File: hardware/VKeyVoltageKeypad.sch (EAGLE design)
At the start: 43 parts, among them IC1 OPAMP-DUALU

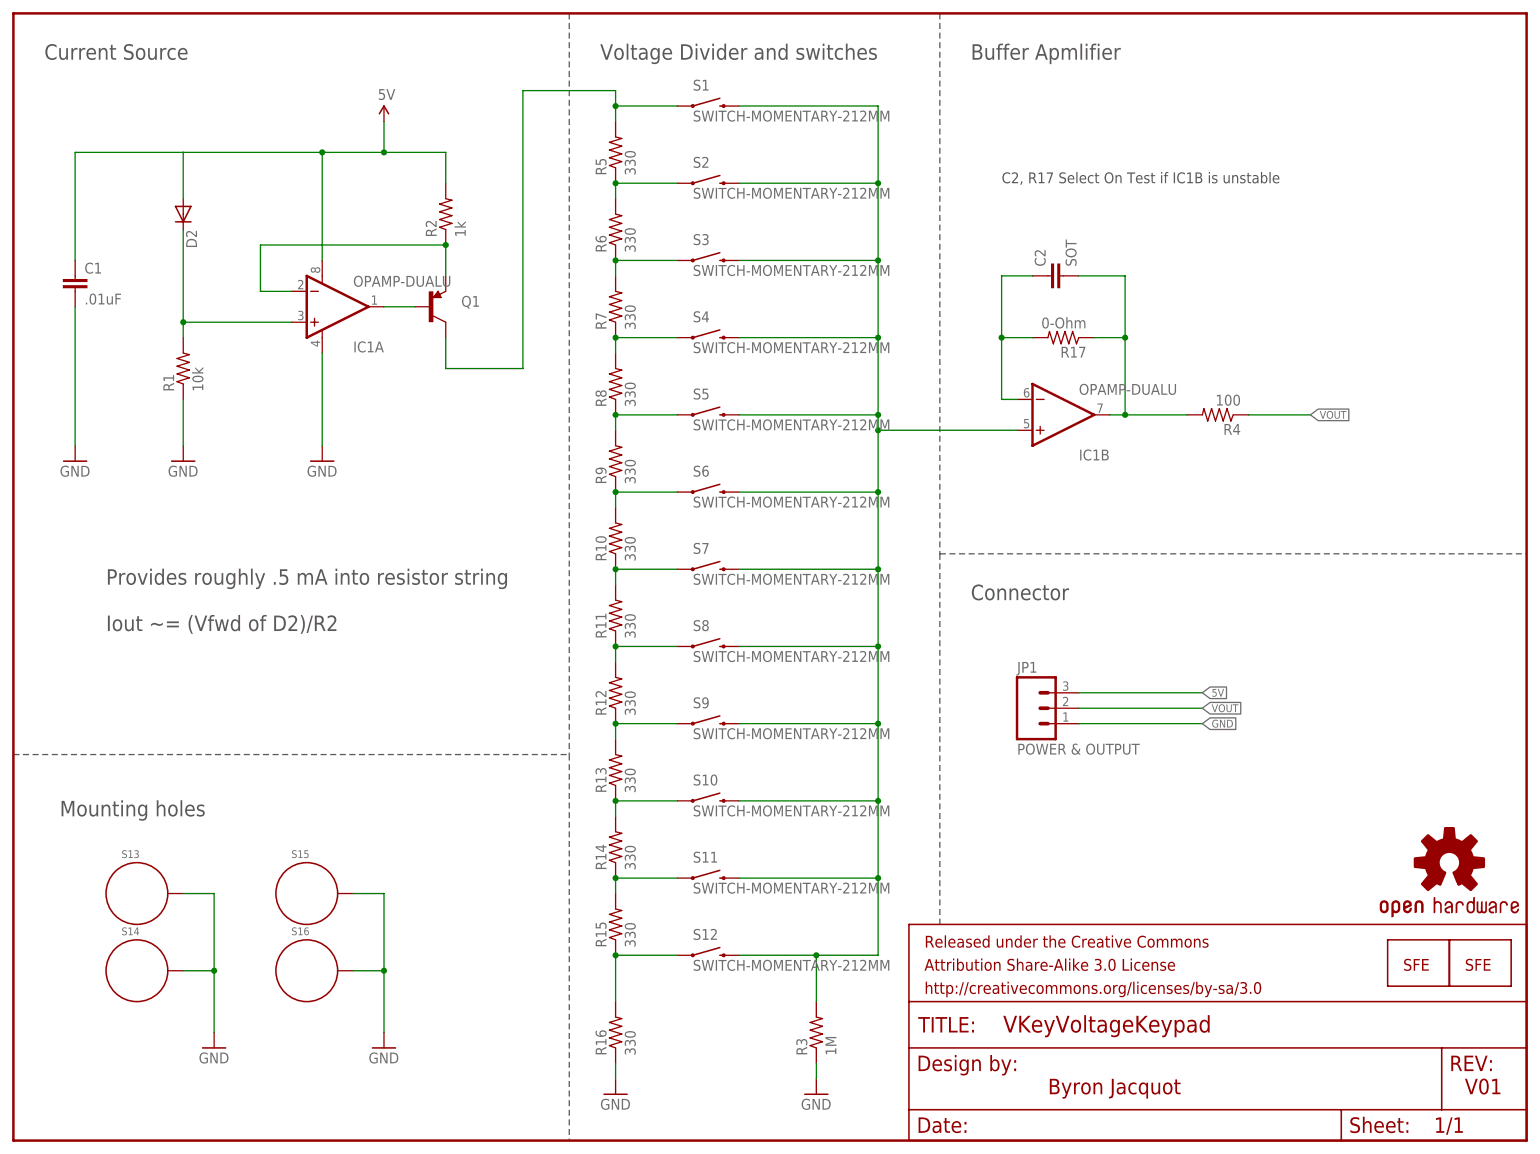
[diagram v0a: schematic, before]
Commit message: Dressing up based on prototype review.
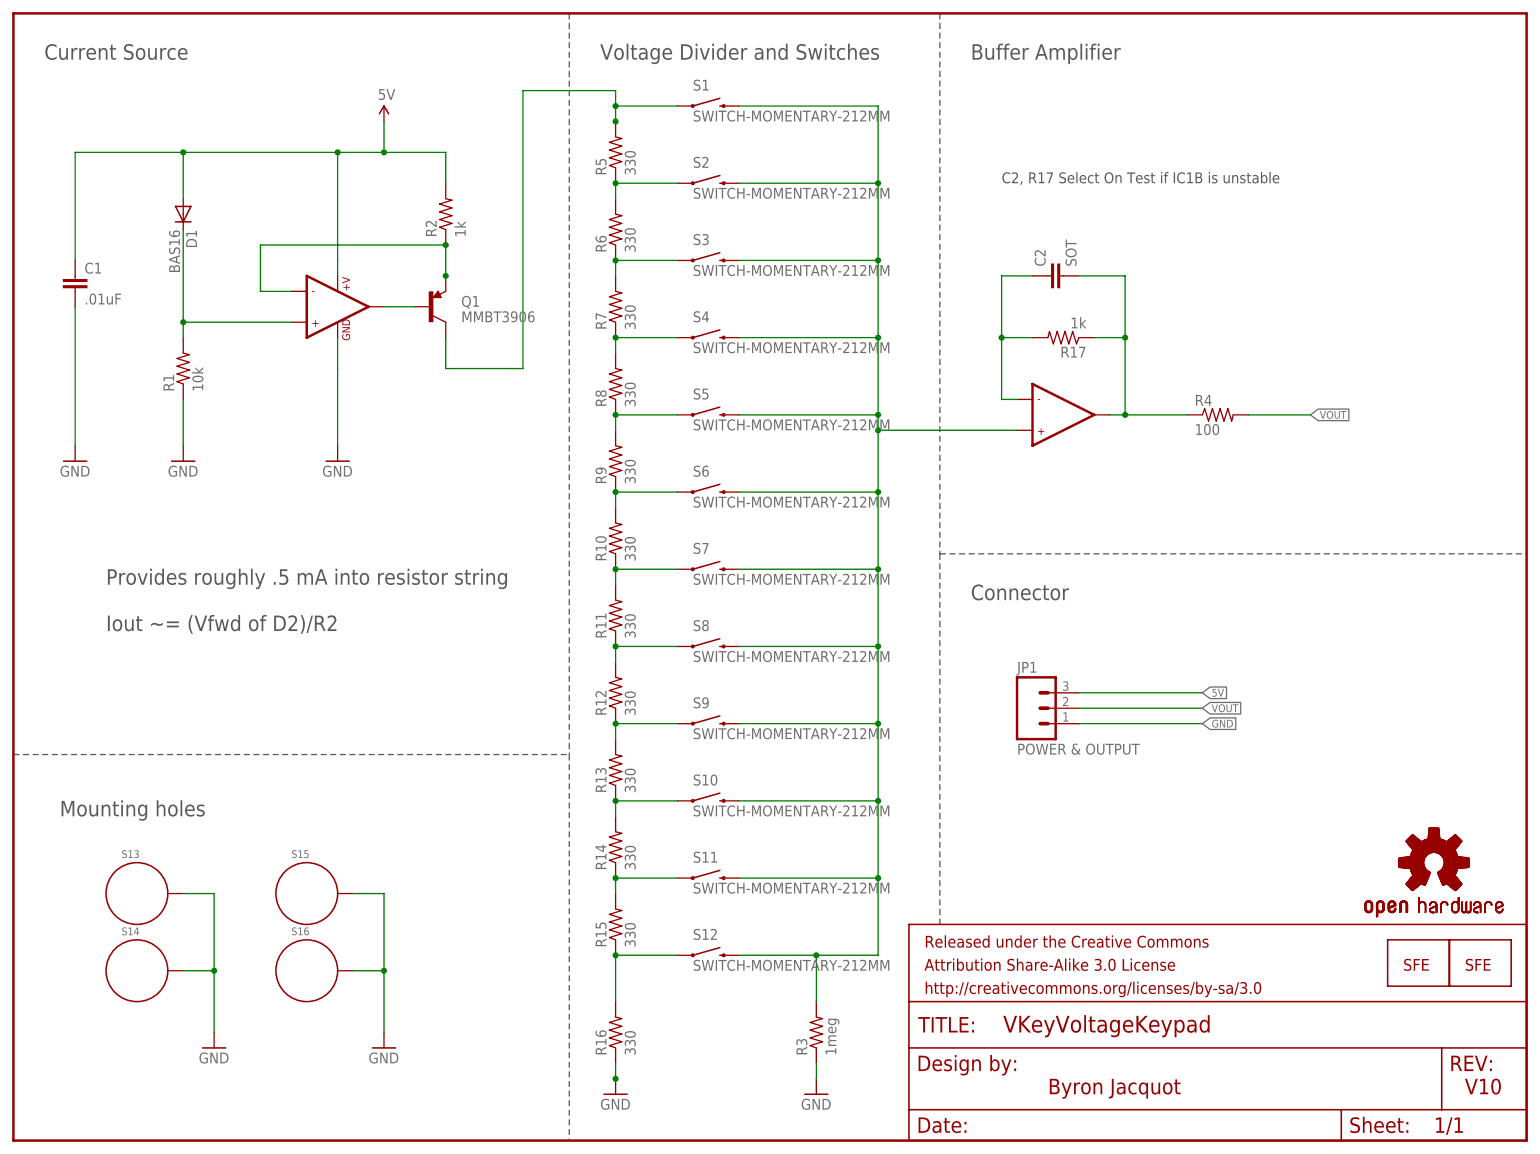
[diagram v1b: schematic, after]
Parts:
- removed D2: (no value), SparkFun-DiscreteSemi:DIODESMA
- removed IC1: OPAMP-DUALU, SparkFun-AnalogIC:OPAMP-DUALU
- added D1: BAS16, SparkFun-DiscreteSemi:DIODESOD
- added LOGO4: OSHW-LOGOL, SparkFun-Aesthetics:OSHW-LOGOL
- added U1: LMV358, SparkFun-AnalogIC:LMV358
- JP1: device SparkFun-Connectors:M03JST-PTH -> SparkFun-Connectors:M031X03_NO_SILK
- Q1: value (none) -> MMBT3906
- R1: device SparkFun-Passives:RESISTOR0603-RES -> SparkFun-Resistors:10KOHM1/10W1%(0603)0603
- R10, R11, R12, R13, R14, R15, R16, R6, R7, R8, R9: device SparkFun-Passives:RESISTOR0603-RES -> SparkFun-Resistors:330OHM1/10W1%(0603); PROD_ID (none) -> RES-00818; VALUE (none) -> 330
- R17: value 0-Ohm -> 1k; device SparkFun-Passives:RESISTOR0603-RES -> SparkFun-Resistors:1KOHM1/10W1%(0603)
- R2: device SparkFun-Passives:RESISTOR0603-RES -> SparkFun-Resistors:1KOHM1/10W1%(0603)
- R3: value 1M -> 1meg; device SparkFun-Passives:RESISTOR0603-RES -> SparkFun-Resistors:1M-1%
- R4: device SparkFun-Passives:RESISTOR0603-RES -> SparkFun-Resistors:100OHM1/10W1%(0603)
- R5: device SparkFun-Passives:RESISTOR0603-RES -> SparkFun-Resistors:330OHM1/10W1%(0603)
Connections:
- net 5V: now also D1.A, U1G$1.+V; no longer D2.A, IC1A.V+
- net GND: now also U1G$1.GND; no longer IC1A.V-
- net N$1: now also D1.C, U1G$1.+IN1; no longer D2.C, IC1A.+IN
- net N$17: now also R4.1, U1G$2.OUT2; no longer IC1B.OUT, R4.2
- net N$18: now also U1G$2.-IN2; no longer IC1B.-IN
- net N$2: now also U1G$1.OUT1; no longer IC1A.OUT
- net N$3: now also U1G$2.+IN2; no longer IC1B.+IN
- net N$5: now also U1G$1.-IN1; no longer IC1A.-IN
- net VOUT: now also R4.2; no longer R4.1
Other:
- note added: "Buffer Amplifier"
- note added: "V10"
- note added: "Voltage Divider and Switches"
- note removed: "Buffer Apmlifier"
- note removed: "V01"
- note removed: "Voltage Divider and switches"
- moved on the sheet: R4

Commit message: Updates post review, moving to v10.
Deleted C2,
Moved connector to very edge of board.
Put connector labels in tPlace.
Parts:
- removed C2: SOT, SparkFun-Capacitors:CAP0603-CAP
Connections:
- net N$17: no longer C2.2
- net N$18: no longer C2.1
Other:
- note removed: "C2, R17 Select On Test if IC1B is unstable"
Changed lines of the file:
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@@
 <part name="C1" library="SparkFun-Capacitors" deviceset="10NF/10000PF-50V-10%(0603)" device="" value=".01uF"/>
 <part name="GND7" library="SparkFun-Aesthetics" deviceset="GND" device=""/>
-<part name="C2" library="SparkFun-Capacitors" deviceset="CAP" device="0603-CAP" value="SOT"/>
 <part name="LOGO2" library="SparkFun-Aesthetics" deviceset="LOGO-SFE" device="NEW"/>
 <part name="LOGO3" library="SparkFun-Aesthetics" deviceset="OSHW-LOGO" device="M"/>
@@
 <plain>
 <text x="238.76" y="7.62" size="2.54" layer="94">V10</text>
-<text x="162.56" y="157.48" size="1.778" layer="97">C2, R17 Select On Test if IC1B is unstable</text>
 <wire x1="0" y1="63.5" x2="91.44" y2="63.5" width="0.1524" layer="97" style="longdash"/>
 <wire x1="91.44" y1="185.42" x2="91.44" y2="63.5" width="0.1524" layer="97" style="longdash"/>
@@
 <instance part="C1" gate="G$1" x="10.16" y="139.7"/>
 <instance part="GND7" gate="1" x="10.16" y="111.76"/>
-<instance part="C2" gate="G$1" x="172.72" y="142.24" rot="R90"/>
 <instance part="LOGO2" gate="G$1" x="228.6" y="27.94"/>
 <instance part="LOGO3" gate="G$1" x="233.68" y="45.72"/>
@@
 <wire x1="182.88" y1="119.38" x2="193.04" y2="119.38" width="0.1524" layer="91"/>
 <junction x="182.88" y="119.38"/>
-<pinref part="C2" gate="G$1" pin="2"/>
-<wire x1="182.88" y1="132.08" x2="182.88" y2="142.24" width="0.1524" layer="91"/>
-<wire x1="182.88" y1="142.24" x2="175.26" y2="142.24" width="0.1524" layer="91"/>
 <wire x1="177.8" y1="132.08" x2="182.88" y2="132.08" width="0.1524" layer="91"/>
-<junction x="182.88" y="132.08"/>
 <pinref part="R17" gate="G$1" pin="1"/>
 <pinref part="R4" gate="G$1" pin="1"/>
@@
 <segment>
 <wire x1="165.1" y1="121.92" x2="162.56" y2="121.92" width="0.1524" layer="91"/>
-<pinref part="C2" gate="G$1" pin="1"/>
-<wire x1="167.64" y1="142.24" x2="162.56" y2="142.24" width="0.1524" layer="91"/>
-<wire x1="162.56" y1="142.24" x2="162.56" y2="132.08" width="0.1524" layer="91"/>
 <wire x1="167.64" y1="132.08" x2="162.56" y2="132.08" width="0.1524" layer="91"/>
-<junction x="162.56" y="132.08"/>
 <wire x1="162.56" y1="132.08" x2="162.56" y2="121.92" width="0.1524" layer="91"/>
 <pinref part="R17" gate="G$1" pin="2"/>

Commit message: Added fiducials to board. Created Panel
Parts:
- added FID1, FID2: FIDUCIALUFIDUCIAL, SparkFun-Aesthetics:FIDUCIALUFIDUCIAL
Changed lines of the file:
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@@
 <?xml version="1.0" encoding="utf-8"?>
 <!DOCTYPE eagle SYSTEM "eagle.dtd">
-<eagle version="6.0">
+<eagle version="6.5.0">
 <drawing>
 <settings>
@@
 <part name="D1" library="SparkFun-DiscreteSemi" deviceset="DIODE" device="SOD" value="BAS16"/>
 <part name="LOGO4" library="SparkFun-Aesthetics" deviceset="OSHW-LOGO" device="L"/>
+<part name="FID1" library="SparkFun-Aesthetics" deviceset="FIDUCIAL" device="UFIDUCIAL"/>
+<part name="FID2" library="SparkFun-Aesthetics" deviceset="FIDUCIAL" device="UFIDUCIAL"/>
 </parts>
 <sheets>
@@
 <instance part="D1" gate="G$1" x="27.94" y="152.4" rot="R270"/>
 <instance part="LOGO4" gate="G$1" x="233.68" y="45.72"/>
+<instance part="FID1" gate="G$1" x="200.66" y="38.1"/>
+<instance part="FID2" gate="G$1" x="205.74" y="38.1"/>
 </instances>
 <busses>
